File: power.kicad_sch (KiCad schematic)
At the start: 38 parts, among them J10 Conn_01x02, J14 Conn_01x02, J25 Conn_01x02, J26 Conn_01x02, J9 Conn_01x02, Q1 2N7002, SW4 SW_SPDT, U1 AP2112K-3.3, U12 Ag9905LP

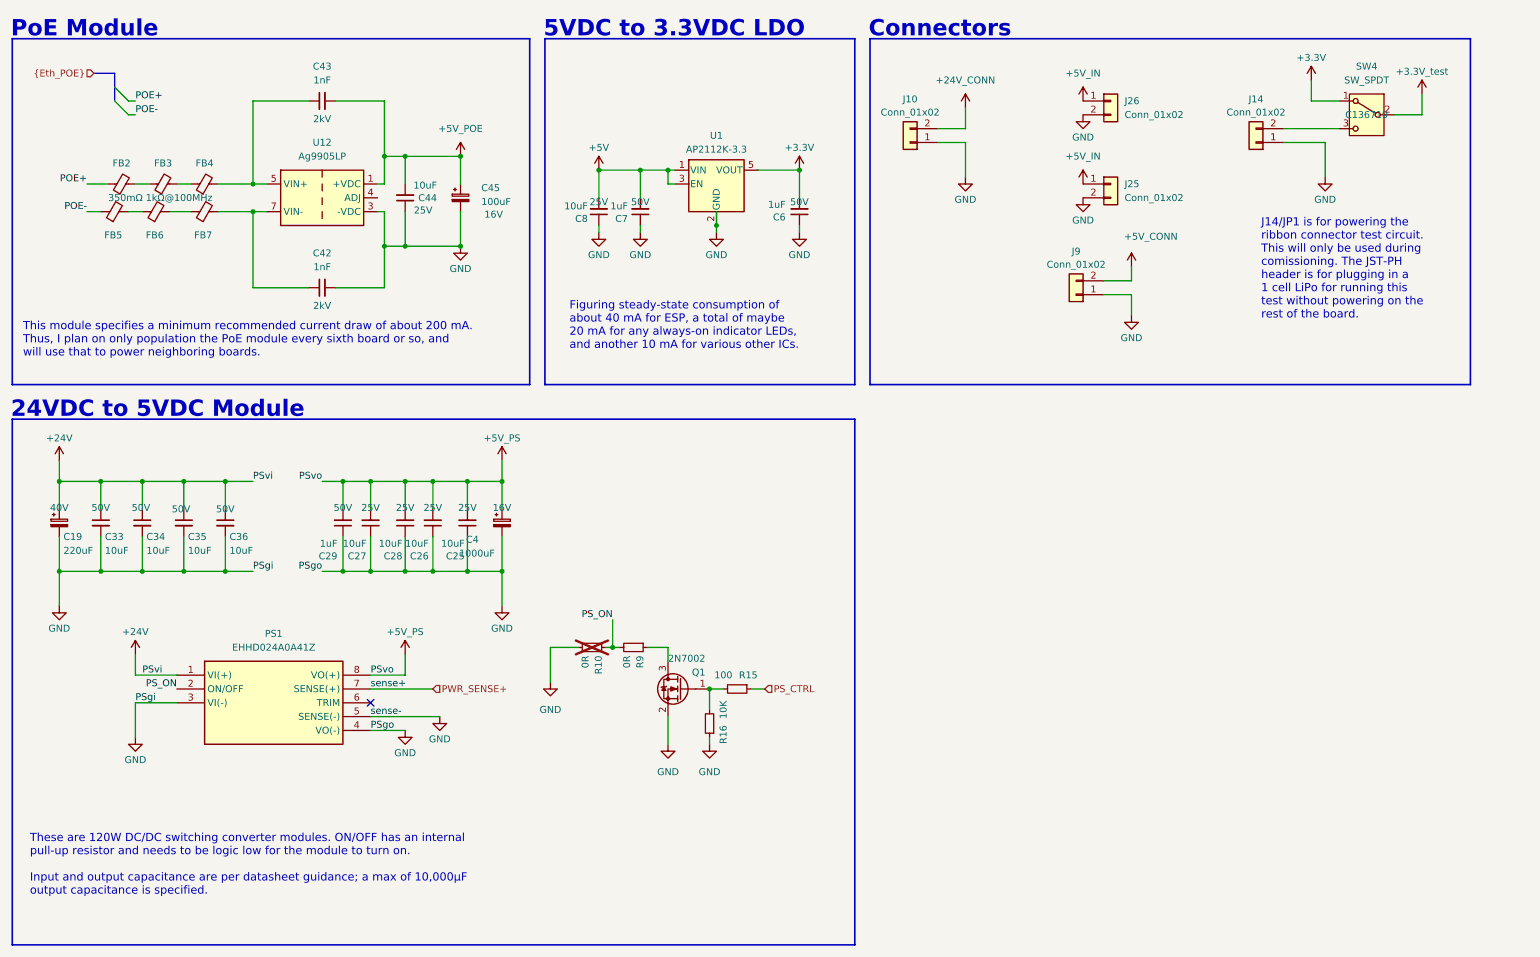
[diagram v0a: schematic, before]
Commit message: schematic annotation
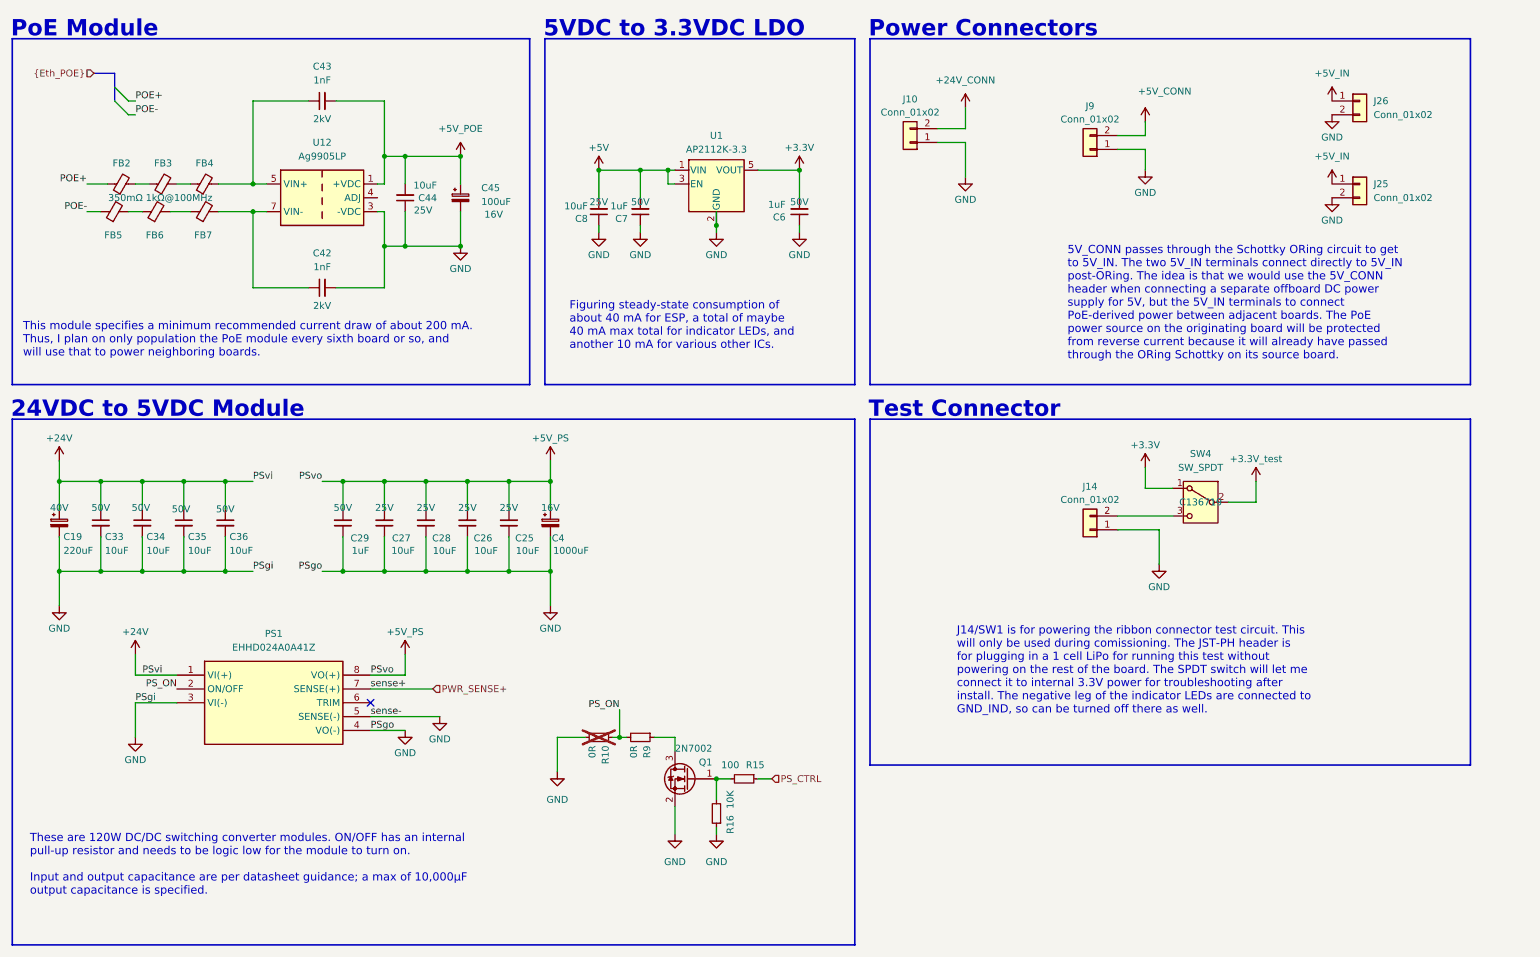
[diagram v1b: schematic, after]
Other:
- note added: "Power Connectors"
- note added: "Test Connector"
- note removed: "Connectors"
- moved on the sheet: C25, C26, C27, C28, C4, J14, J25, J26, J9, Q1, R10, R15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

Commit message: MOAR STITCHING and some cleanup
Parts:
- J25, J26: footprint (none) -> easyeda2kicad:CONN-TH_2P-MX250-3.5-02P-B-GY01-CU-A; LCSC (none) -> C7470116
- J9: footprint easyeda2kicad:CONN-TH_P5.00_KF243-5.0-2P -> easyeda2kicad:CONN-TH_2P-MX250-3.5-02P-B-GY01-CU-A; LCSC C475222 -> C7470116
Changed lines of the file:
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@@
 			)
 		)
-		(property "Footprint" ""
+		(property "Footprint" "easyeda2kicad:CONN-TH_2P-MX250-3.5-02P-B-GY01-CU-A"
 			(at 261.62 48.26 0)
 			(effects
@@
 				)
 				(hide yes)
+			)
+		)
+		(property "LCSC" "C7470116"
+			(at 261.62 48.26 0)
+			(effects
+				(font
+					(size 1.27 1.27)
+				)
 			)
 		)
@@
 			)
 		)
-		(property "Footprint" ""
+		(property "Footprint" "easyeda2kicad:CONN-TH_2P-MX250-3.5-02P-B-GY01-CU-A"
 			(at 261.62 33.02 0)
 			(effects
@@
 				)
 				(hide yes)
+			)
+		)
+		(property "LCSC" "C7470116"
+			(at 261.62 33.02 0)
+			(effects
+				(font
+					(size 1.27 1.27)
+				)
 			)
 		)
@@
 			)
 		)
-		(property "Footprint" "easyeda2kicad:CONN-TH_P5.00_KF243-5.0-2P"
+		(property "Footprint" "easyeda2kicad:CONN-TH_2P-MX250-3.5-02P-B-GY01-CU-A"
 			(at 212.09 41.91 0)
 			(effects
@@
 			)
 		)
-		(property "LCSC" "C475222"
+		(property "LCSC" "C7470116"
 			(at 212.09 41.91 0)
 			(effects
